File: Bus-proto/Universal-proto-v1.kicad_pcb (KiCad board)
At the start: 2 copper layers, 81.5 x 121 mm, 51 parts, among them J1 Bus_ISA_8bit, J2 ISA Breakout, J3 Pico GPIO Breakout 2, J4 Pico GPIO Breakout 1, J5 Conn_01x20, J6 Conn_01x20, J7 Conn_01x20, J8 Conn_01x20, J9 Conn_02x02_Odd_Even

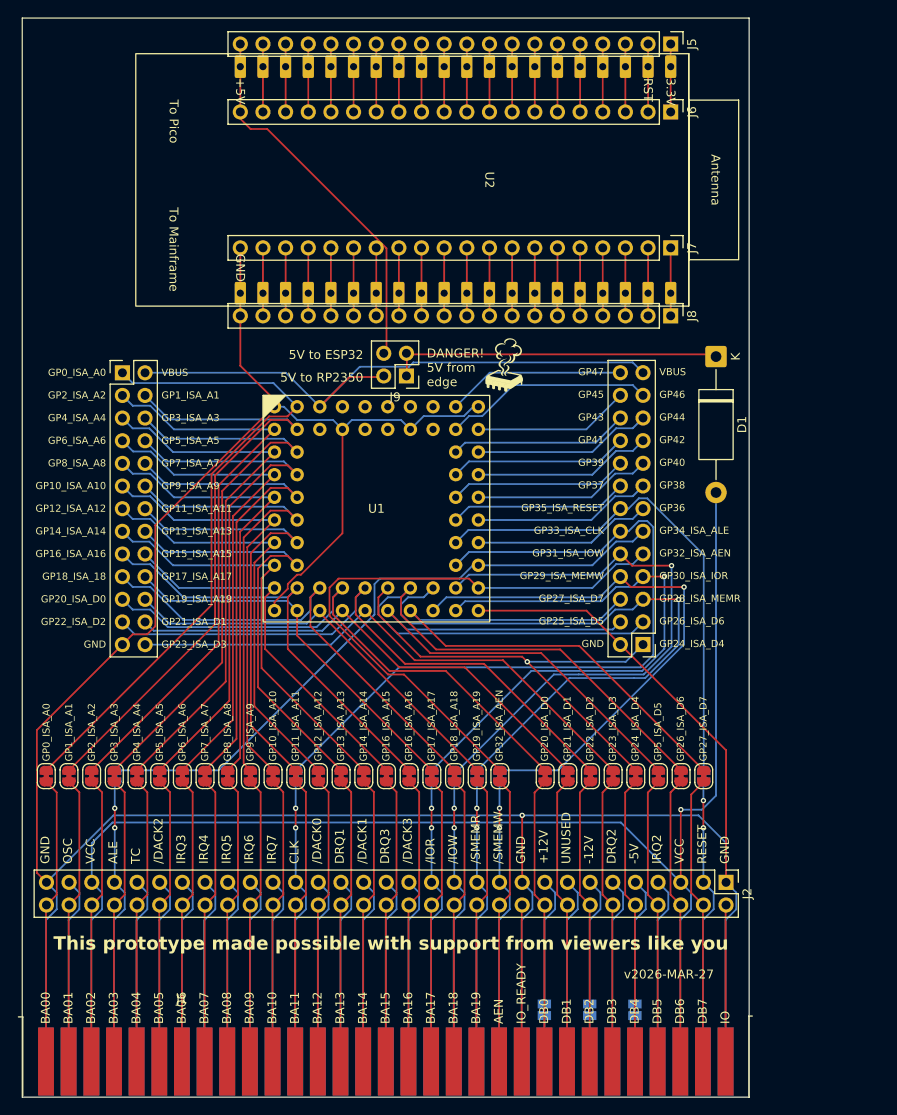
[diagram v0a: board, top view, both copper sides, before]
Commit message: Add MSX adapter
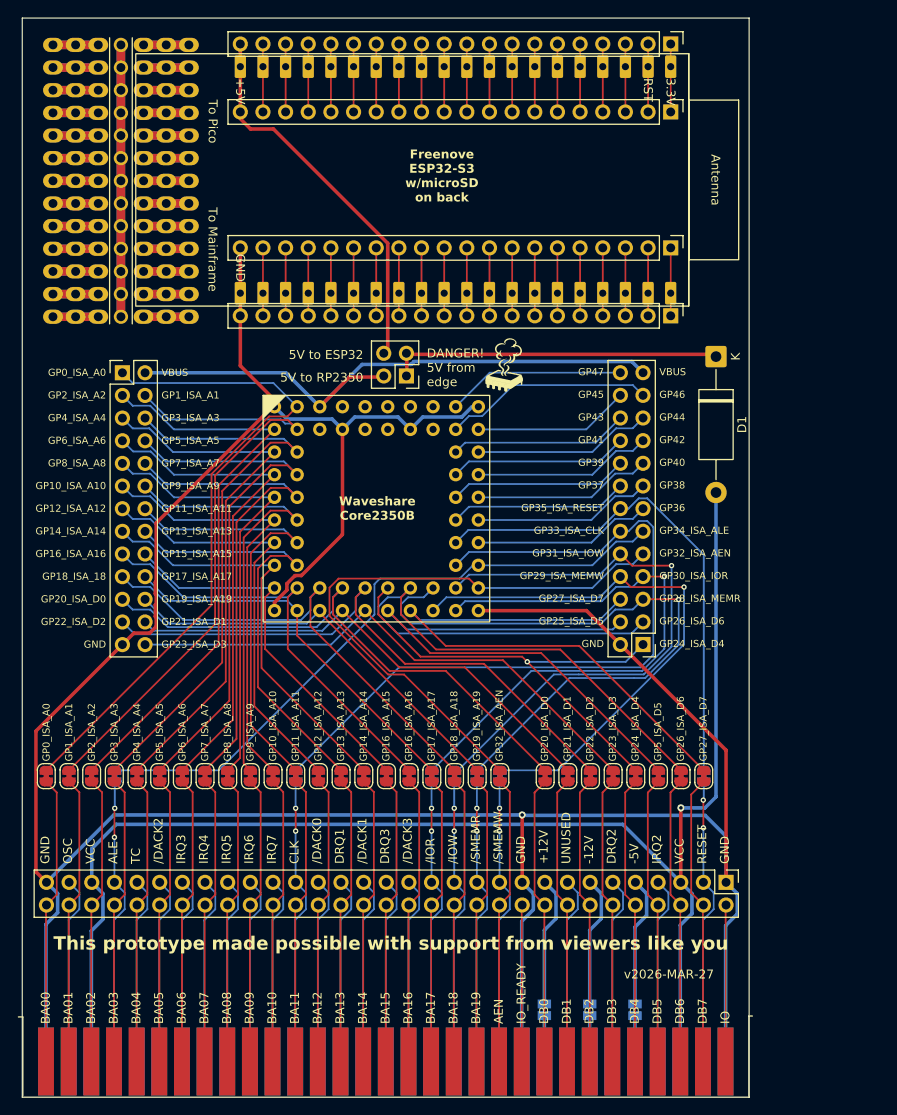
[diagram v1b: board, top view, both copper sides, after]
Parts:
- added REF**: StripGrid_7x13, parts:StripGrid_7x13, F.Cu at (118.1, 41.2)
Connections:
- net Net-(D1-K) renamed /VCC_D
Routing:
- net /GND: track 338.8 -> 340.4 mm
- net /E_5V: track 42.0 -> 42.8 mm
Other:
- board text added: "Freenove ESP32-S3 w/microSD on back"
- board text added: "Waveshare Core2350B"
